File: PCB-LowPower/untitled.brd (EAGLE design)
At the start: 155 x 79 mm, 23 parts, among them J1 RJ45-8N-B, J2 22-27-2041-04, U1 ESP32-DEVKITC-32D, X1 MSTBA2

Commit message: revisi PCB
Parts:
- added J3: 22-27-2051-05, con-molex:6410-05
- moved S1 2.00 mm to (6.17, 2.23)
- moved S2 2.00 mm to (16.1, 2.23)
- moved J1 2.00 mm to (48.7, 75.3)
- moved S3 2.00 mm to (76.8, 2.00)
- moved U$2 2.00 mm to (15.1, 81.1)
- moved X1 2.00 mm to (65.4, 79.1)
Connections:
- net 3V3: now also J3.5
- net GND: now also J3.1
- net P2_1: now also J3.4; no longer U1.29
- net P2_2: now also J3.3; no longer U1.34
- net RST_Z: now also J3.2
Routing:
- net RST_Z: track 28.9 -> 112.3 mm
- net GND: track 419.3 -> 443.0 mm
- net P2_2: track 34.9 -> 56.5 mm
- net 3V3: track 191.0 -> 204.8 mm, vias 2 -> 3
- net P2_1: track 37.0 -> 49.9 mm
- net MOSI_HSPI: track 88.8 -> 91.3 mm
- net SCK_HSPI: track 83.5 -> 85.8 mm
- net N$2: track 26.6 -> 24.5 mm
- net N$3: track 32.7 -> 34.7 mm
- net EN: track 84.7 -> 86.7 mm
- net N$1: track 9.29 -> 10.8 mm
- net OUT+: track 217.7 -> 218.8 mm
- net N$7: track 63.6 -> 62.5 mm
- net SS_LAN: track 87.9 -> 88.8 mm
- net MISO_HSPI: track 204.1 -> 204.9 mm
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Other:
- board size 155 x 79 mm -> 155 x 83 mm

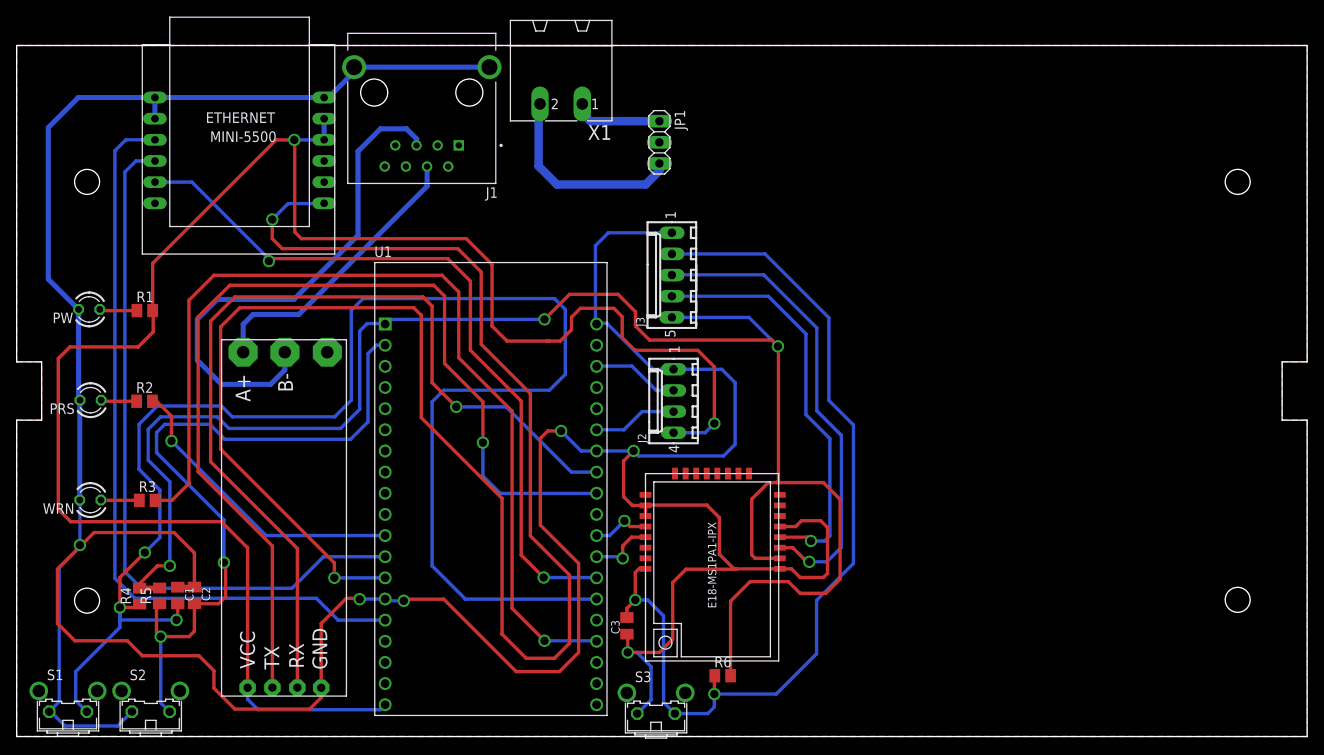
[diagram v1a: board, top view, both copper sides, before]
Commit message: menambahkan rangkaian PCB TOP
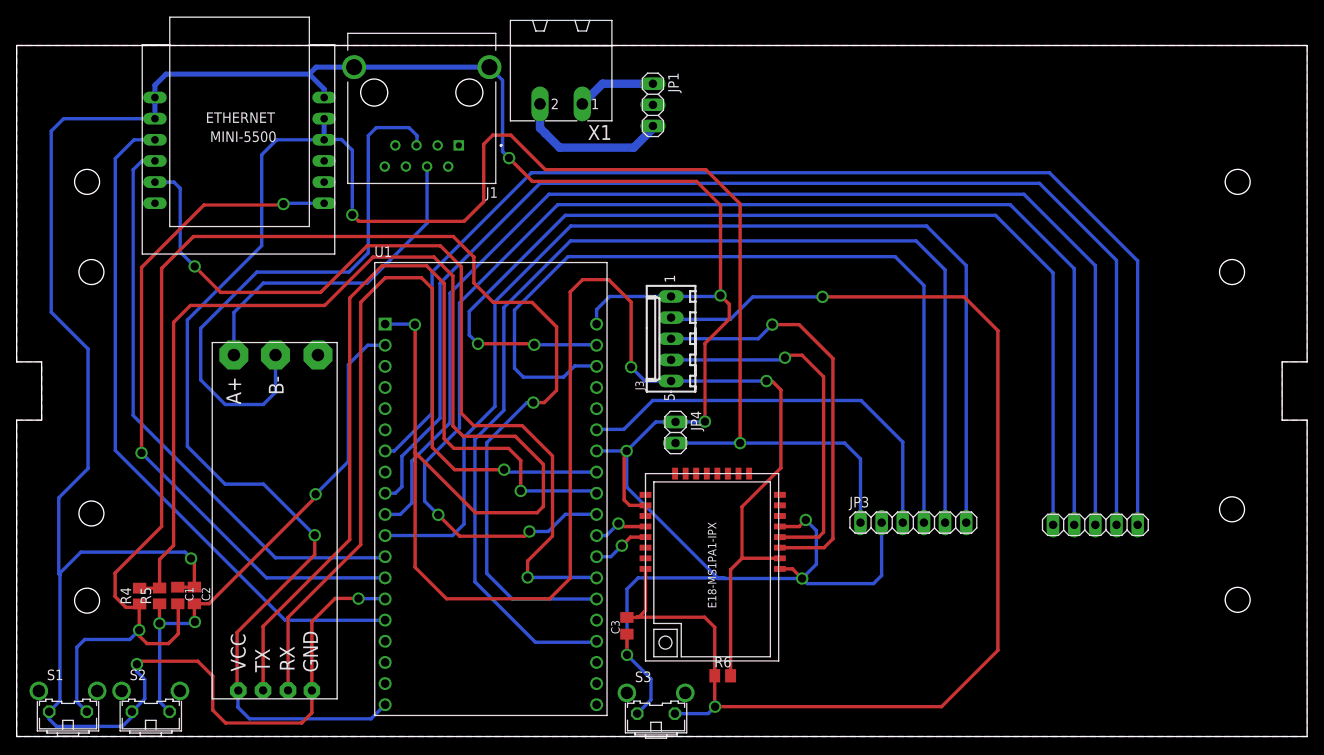
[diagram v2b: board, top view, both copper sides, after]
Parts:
- removed J2: 22-27-2041-04, con-molex:6410-04
- removed PRS, PW, WRN: TLLR4400, led:LED3MM
- removed R1, R2, R3: 330, adafruit:M0805
- added JP2: (no value), pinhead:1X05
- added JP3: (no value), pinhead:1X06
- added JP4: (no value), pinhead:1X02
- moved J3 7.65 mm to (78.6, 45.8)
- moved JP1 4.57 mm to (76.4, 73.9)
- moved TTL-RS1 1.17 mm to (32.1, 24.1)
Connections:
- removed net N$4: PW.A, R1.1
- removed net N$5: PRS.A, R2.1
- removed net N$6: R3.1, WRN.A
- new net DWN: JP2.4, U1.29
- new net LFT: JP2.3, U1.10
- new net MID: JP2.1, U1.7
- new net RHT: JP2.2, U1.9
- new net UP: JP2.5, U1.21
- net GND: now also JP3.2, JP4.1; no longer J2.1, PRS.K, PW.K, WRN.K
- net LED_PROSES: now also JP3.6; no longer R2.2
- net LED_WARNING: now also JP3.5; no longer R3.2
- net OUT+: now also JP3.1, JP4.2; no longer J2.4, R1.2
- net SCL: now also JP3.4; no longer J2.2
- net SDA: now also JP3.3; no longer J2.3
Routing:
- net DWN: track 0.00 -> 161.7 mm, vias 0 -> 2
- net RHT: track 0.00 -> 150.8 mm
- net MID: track 0.00 -> 150.2 mm
- net LFT: track 0.00 -> 148.2 mm
- net UP: track 0.00 -> 126.7 mm, vias 0 -> 2
- net MISO_HSPI: track 204.9 -> 83.0 mm
- net LED_PROSES: track 36.4 -> 131.5 mm, vias 1 -> 0
- net SCL: track 10.5 -> 99.6 mm
- net 3V3: track 204.8 -> 293.2 mm
- net SDA: track 10.1 -> 50.0 mm
- net RST_Z: track 112.3 -> 149.5 mm
- net LED_WARNING: track 113.8 -> 140.2 mm, vias 1 -> 0
- net EN: track 86.7 -> 62.8 mm, vias 2 -> 3
- net OUT+: track 218.8 -> 242.5 mm, vias 2 -> 3
- net SS_LAN: track 88.8 -> 104.9 mm
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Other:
- outline, holes or cut-outs redrawn
